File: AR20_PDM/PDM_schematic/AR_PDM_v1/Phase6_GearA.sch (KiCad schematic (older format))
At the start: 15 parts, among them Q17 N_FET, Q6 BTS50025-1TAD, U8 INA233

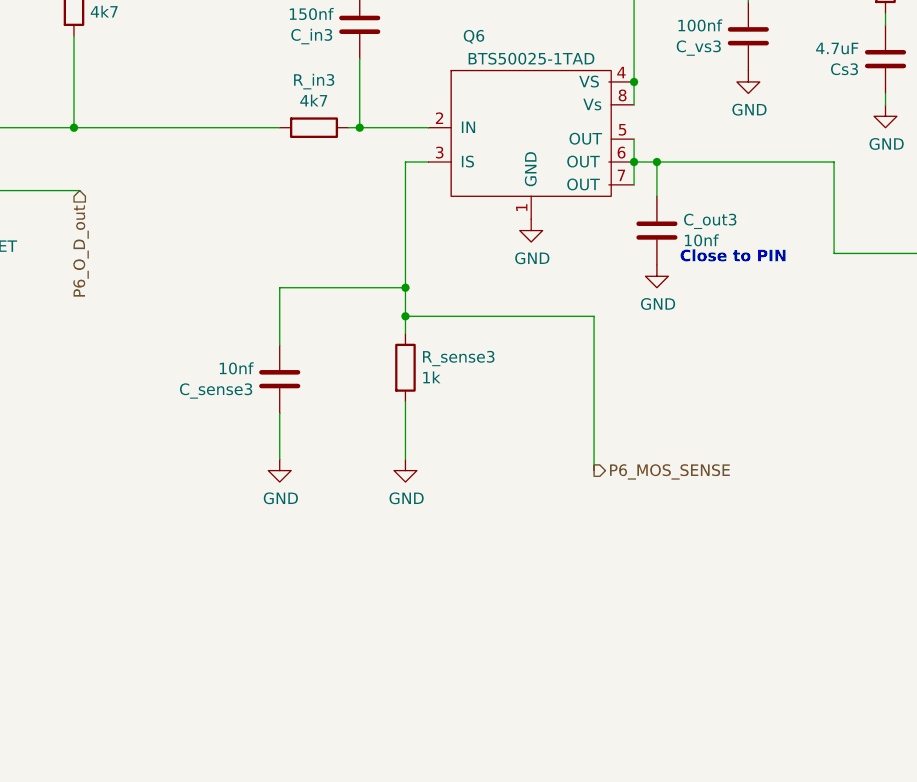
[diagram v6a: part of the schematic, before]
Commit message: PCB Design,  minor schematics changes, work in progress, see description
- Removed mos sense caps and resistors accept one, 
since only one measurement can be done, at a time.
- added mos sens protection resistors on each line, to protect mux mosfets and micro controller. 
- Routing plan mostly finalized, some of the traces are just proof of concept.
those needs to be routed nicely.
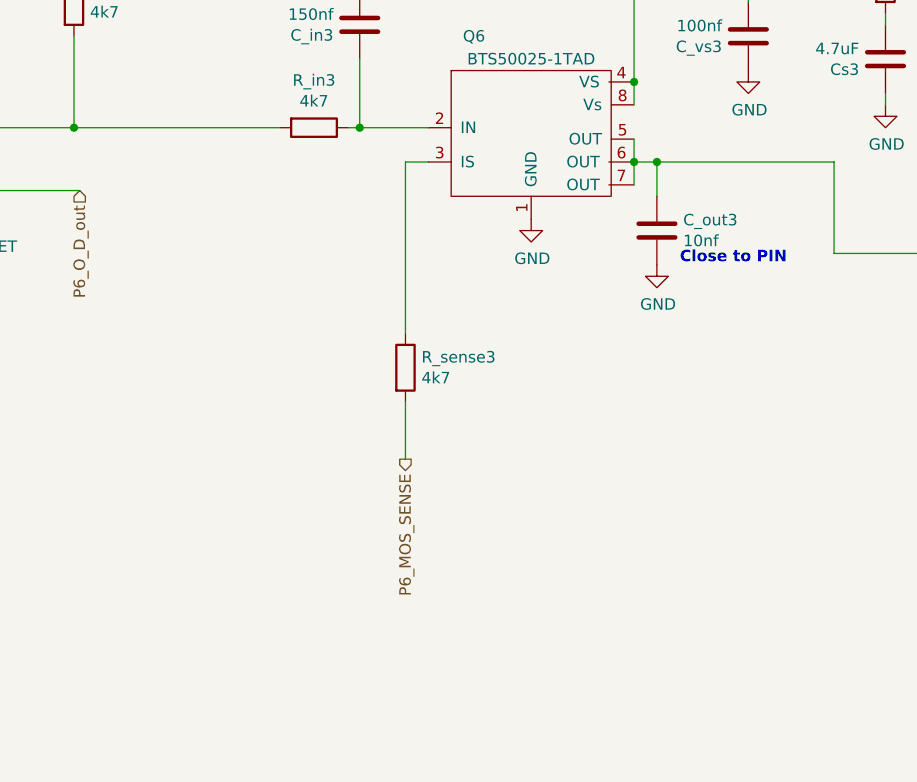
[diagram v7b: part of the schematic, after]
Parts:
- removed C_sense3: 10nf, Capacitor_SMD:C_0603_1608Metric, symbol AR20_PDM_v1-rescue:C-Device
- R_sense3: value 1k -> 4k7
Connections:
- net GND: no longer R_sense3.2
- net P6_MOS_SENSE: now also R_sense3.2; no longer Q6.3 (IS), R_sense3.1
- new net: Q6.3 (IS), R_sense3.1
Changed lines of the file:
@@
-$EndComp
-$Comp
-L AR20_PDM_v1-rescue:GND-power #PWR?
-U 1 1 5E21B81F
-P 3700 3850
-AR Path="/5DA89415/5E21B81F" Ref="#PWR?"  Part="1"
-AR Path="/5DEB10A1/5E21B81F" Ref="#PWR?"  Part="1"
-AR Path="/5DEB20EA/5E21B81F" Ref="#PWR?"  Part="1"
-AR Path="/5E0E4725/5E21B81F" Ref="#PWR?"  Part="1"
-AR Path="/5E0E4A93/5E21B81F" Ref="#PWR?"  Part="1"
-AR Path="/5E0E4EB5/5E21B81F" Ref="#PWR?"  Part="1"
-AR Path="/5E0E5304/5E21B81F" Ref="#PWR?"  Part="1"
-AR Path="/5E0E594B/5E21B81F" Ref="#PWR?"  Part="1"
-AR Path="/5E0E607C/5E21B81F" Ref="#PWR?"  Part="1"
-AR Path="/5E0FB5C8/5E21B81F" Ref="#PWR?"  Part="1"
-AR Path="/5E0FBBBD/5E21B81F" Ref="#PWR?"  Part="1"
-AR Path="/5E0FC3A2/5E21B81F" Ref="#PWR?"  Part="1"
-AR Path="/5E0FCFDC/5E21B81F" Ref="#PWR?"  Part="1"
-AR Path="/5E0FDCCC/5E21B81F" Ref="#PWR056"  Part="1"
-AR Path="/5E10174B/5E21B81F" Ref="#PWR?"  Part="1"
-F 0 "#PWR056" H 3700 3600 50  0001 C CNN
-F 1 "GND" H 3705 3677 50  0000 C CNN
-F 2 "" H 3700 3850 50  0001 C CNN
-F 3 "" H 3700 3850 50  0001 C CNN
-	1    3700 3850
-	1    0    0    -1
 $EndComp
 $Comp
@@
 $EndComp
 Wire Wire Line
-	3700 2550 3700 3100
-Wire Wire Line
 	3700 2550 3800 2550
 Wire Wire Line
@@
 Wire Wire Line
 	9700 4450 10000 4450
-$Comp
-L AR20_PDM_v1-rescue:GND-power #PWR?
-U 1 1 5E21B84B
-P 3150 3850
-AR Path="/5DA89415/5E21B84B" Ref="#PWR?"  Part="1"
-AR Path="/5DEB10A1/5E21B84B" Ref="#PWR?"  Part="1"
-AR Path="/5DEB20EA/5E21B84B" Ref="#PWR?"  Part="1"
-AR Path="/5E0E4725/5E21B84B" Ref="#PWR?"  Part="1"
-AR Path="/5E0E4A93/5E21B84B" Ref="#PWR?"  Part="1"
-AR Path="/5E0E4EB5/5E21B84B" Ref="#PWR?"  Part="1"
-AR Path="/5E0E5304/5E21B84B" Ref="#PWR?"  Part="1"
-AR Path="/5E0E594B/5E21B84B" Ref="#PWR?"  Part="1"
-AR Path="/5E0E607C/5E21B84B" Ref="#PWR?"  Part="1"
-AR Path="/5E0FB5C8/5E21B84B" Ref="#PWR?"  Part="1"
-AR Path="/5E0FBBBD/5E21B84B" Ref="#PWR?"  Part="1"
-AR Path="/5E0FC3A2/5E21B84B" Ref="#PWR?"  Part="1"
-AR Path="/5E0FCFDC/5E21B84B" Ref="#PWR?"  Part="1"
-AR Path="/5E0FDCCC/5E21B84B" Ref="#PWR054"  Part="1"
-AR Path="/5E10174B/5E21B84B" Ref="#PWR?"  Part="1"
-F 0 "#PWR054" H 3150 3600 50  0001 C CNN
-F 1 "GND" H 3155 3677 50  0000 C CNN
-F 2 "" H 3150 3850 50  0001 C CNN
-F 3 "" H 3150 3850 50  0001 C CNN
-	1    3150 3850
-	1    0    0    -1
-$EndComp
-$Comp
-L AR20_PDM_v1-rescue:C-Device C_sense?
-U 1 1 5E21B852
-P 3150 3500
-AR Path="/5DA89415/5E21B852" Ref="C_sense?"  Part="1"
-AR Path="/5DEB10A1/5E21B852" Ref="C_sense?"  Part="1"
-AR Path="/5DEB20EA/5E21B852" Ref="C_sense?"  Part="1"
-AR Path="/5E0E4725/5E21B852" Ref="C_sense?"  Part="1"
-AR Path="/5E0E4A93/5E21B852" Ref="C_sense?"  Part="1"
-AR Path="/5E0E4EB5/5E21B852" Ref="C_sense?"  Part="1"
-AR Path="/5E0E5304/5E21B852" Ref="C_sense?"  Part="1"
-AR Path="/5E0E594B/5E21B852" Ref="C_sense?"  Part="1"
-AR Path="/5E0E607C/5E21B852" Ref="C_sense?"  Part="1"
-AR Path="/5E0FB5C8/5E21B852" Ref="C_sense?"  Part="1"
-AR Path="/5E0FBBBD/5E21B852" Ref="C_sense?"  Part="1"
-AR Path="/5E0FC3A2/5E21B852" Ref="C_sense?"  Part="1"
-AR Path="/5E0FCFDC/5E21B852" Ref="C_sense?"  Part="1"
-AR Path="/5E0FDCCC/5E21B852" Ref="C_sense3"  Part="1"
-AR Path="/5E10174B/5E21B852" Ref="C_sense?"  Part="1"
-F 0 "C_sense3" H 3265 3546 50  0000 L CNN
-F 1 "10nf" H 3265 3455 50  0000 L CNN
-F 2 "Capacitor_SMD:C_0603_1608Metric" H 3188 3350 50  0001 C CNN
-F 3 "~" H 3150 3500 50  0001 C CNN
-	1    3150 3500
-	-1   0    0    1
-$EndComp
 Wire Wire Line
 	3450 2400 3500 2400
@@
 Text Notes 8200 3050 0    50   ~ 10
 Close to PIN
-Wire Wire Line
-	3150 3100 3150 3350
-Wire Wire Line
-	3150 3650 3150 3850
-Wire Wire Line
-	3150 3100 3700 3100
-Connection ~ 3700 3100
-Wire Wire Line
-	3700 3100 3700 3225
 Text HLabel 2250 1550 1    50   Input ~ 10
 vcc_5v
@@
 AR Path="/5E10174B/5E21B873" Ref="R_sense?"  Part="1"
 F 0 "R_sense3" H 3770 3496 50  0000 L CNN
-F 1 "1k" H 3770 3405 50  0000 L CNN
+F 1 "4k7" H 3770 3405 50  0000 L CNN
 F 2 "Resistor_SMD:R_0603_1608Metric" V 3630 3450 50  0001 C CNN
 F 3 "~" H 3700 3450 50  0001 C CNN
@@
 Wire Wire Line
 	6625 4300 8750 4300
-Wire Wire Line
-	3700 3225 4525 3225
-Wire Wire Line
-	4525 3225 4525 3900
-Connection ~ 3700 3225
-Wire Wire Line
-	3700 3225 3700 3300
-Text HLabel 4525 3900 2    50   Output ~ 0
+Text HLabel 3700 3850 3    50   Output ~ 0
 P6_MOS_SENSE
 Wire Wire Line
@@
 P6_Shunt
 Connection ~ 6000 2950
+Wire Wire Line
+	3700 2550 3700 3300
 $EndSCHEMATC

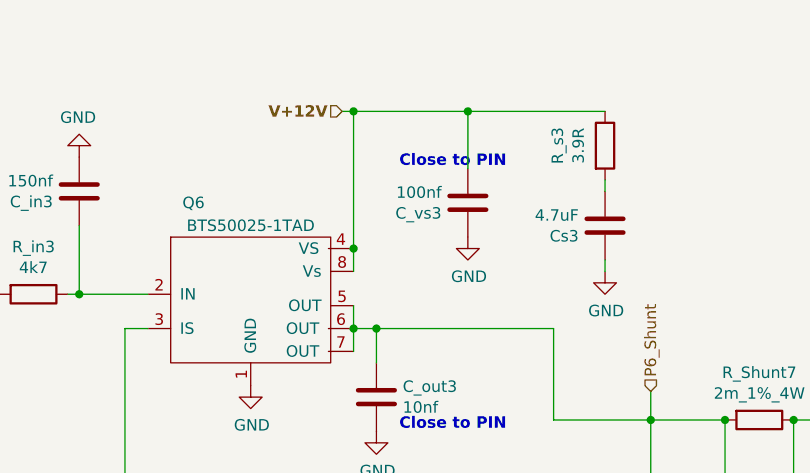
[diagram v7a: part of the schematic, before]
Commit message: First Complete Draft of PCB and schematics, - minus see discription
- missing correct smd switch header
- missing correct main power plug
- tweeks still needs to be done
- Extra inspection of schematics pending
- proper, in depth quiality controll of pcb work pending
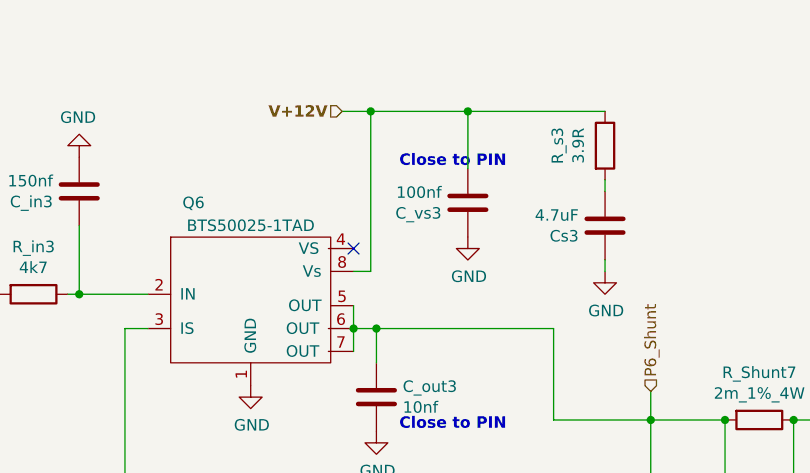
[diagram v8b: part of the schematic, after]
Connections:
- net V+12V: no longer Q6.4 (VS)
- no-connect marks 0 -> 1
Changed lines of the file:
@@
 $Descr A4 11693 8268
 encoding utf-8
-Sheet 6 13
+Sheet 5 13
 Title ""
 Date ""
@@
 vcc_5v
 Wire Wire Line
-	4650 1600 4700 1600
-Wire Wire Line
 	4700 2650 4700 2550
 Connection ~ 4700 2550
 Wire Wire Line
 	4700 2450 4700 2550
-Wire Wire Line
-	4700 2300 4700 2200
-Wire Wire Line
-	4700 2200 4700 1600
-Connection ~ 4700 2200
-Connection ~ 4700 1600
-Wire Wire Line
-	4700 1600 5200 1600
 Text HLabel 2275 2675 3    50   Input ~ 0
 P6_O_D_out
@@
 Wire Wire Line
 	3700 2550 3700 3300
+Wire Wire Line
+	4650 1600 4775 1600
+Wire Wire Line
+	4775 2300 4700 2300
+Wire Wire Line
+	4775 1600 4775 2300
+NoConn ~ 4700 2200
+Connection ~ 4775 1600
+Wire Wire Line
+	4775 1600 5200 1600
 $EndSCHEMATC
